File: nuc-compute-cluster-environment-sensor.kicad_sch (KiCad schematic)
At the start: 122 parts, among them J15 USB-C_GCT_USB4105-GF-A, J16 JST_SH_1x4_SM04B-SRSS-TB-LF-SN, J17 JST_SH_1x4_SM04B-SRSS-TB-LF-SN, U24 FT4232H_VQFN, U25 AP7370-33SA-7, U26 STM32G474CET6, U27 MB85RC1MTPNF-G, U28 SHT45, U29 BME280, Y2 Resonator_12MHz_ABM3B, Y3 Resonator_32.768kHz_ABS06, Y4 Resonator_8MHz_ABM3B

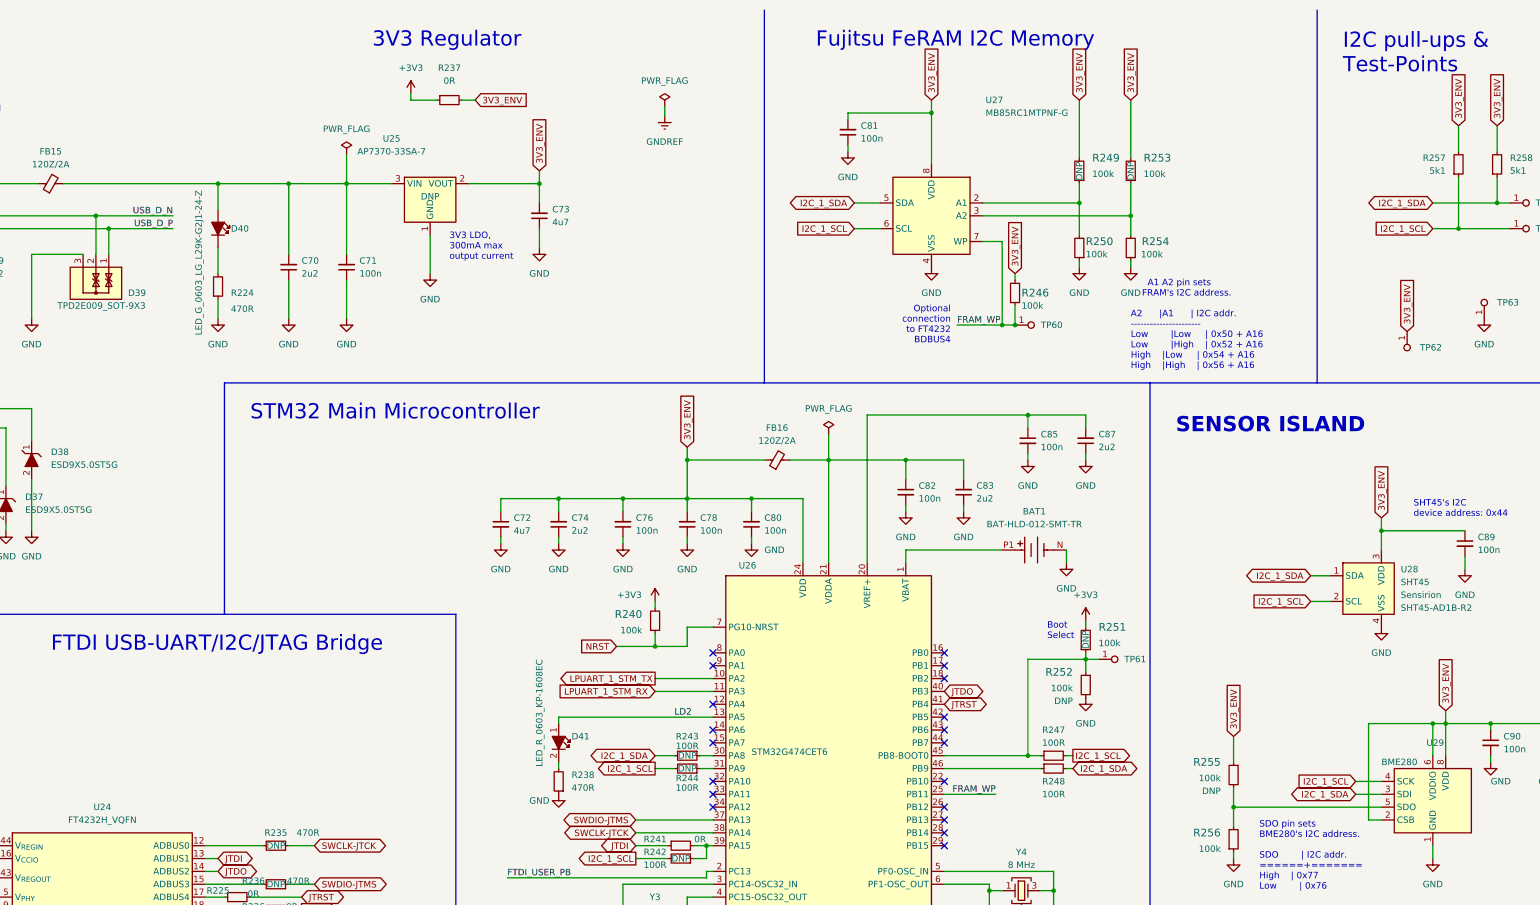
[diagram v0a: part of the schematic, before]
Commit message: Standarize all components and enumerate
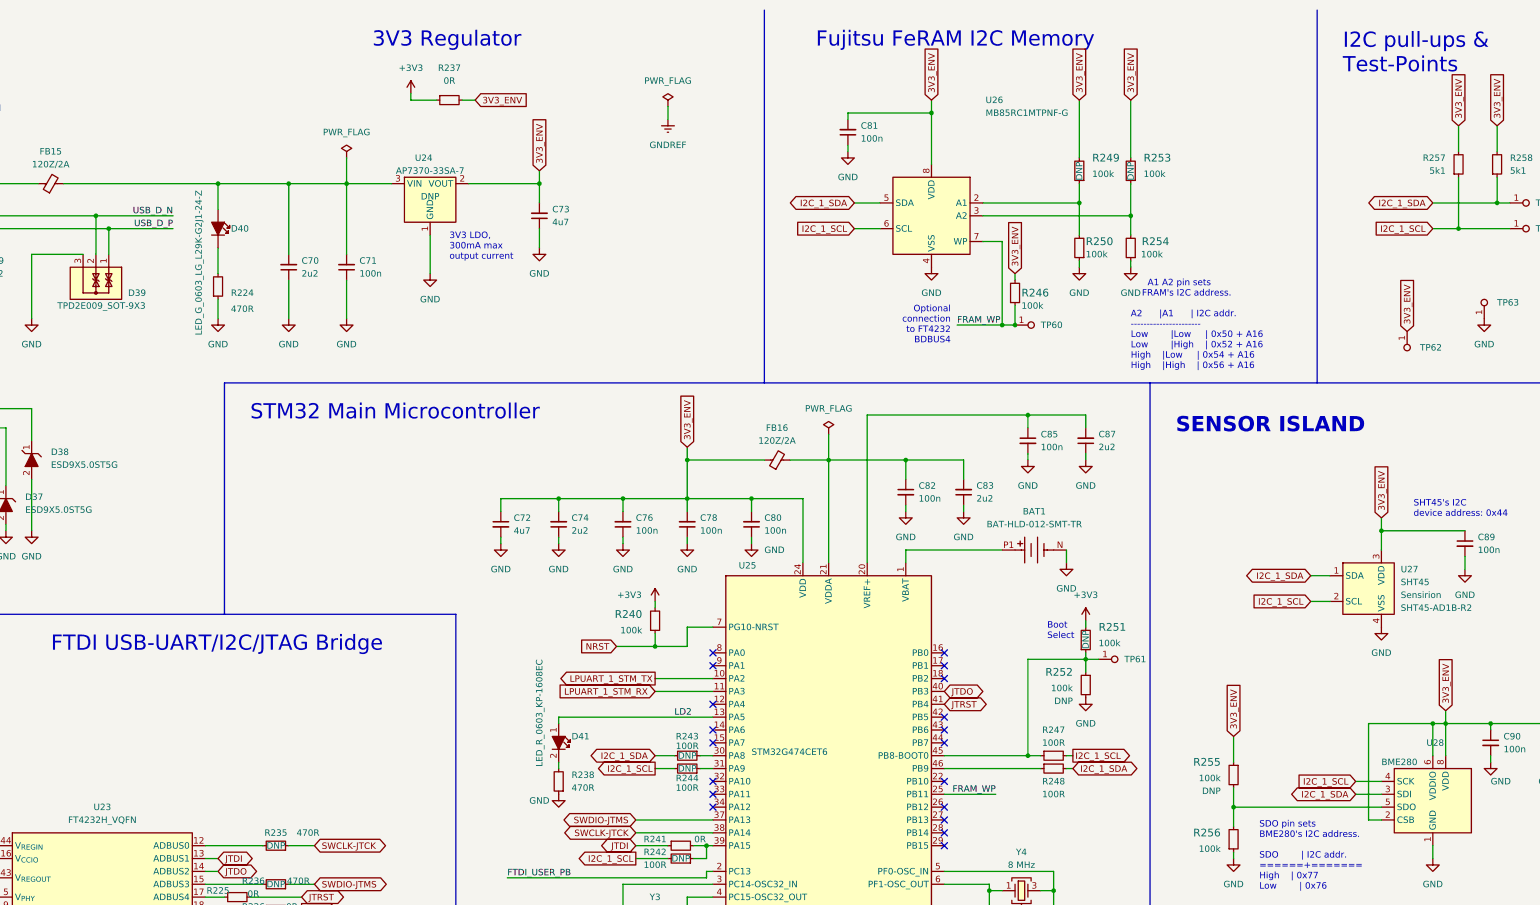
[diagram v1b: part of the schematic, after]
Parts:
- renumbered U24 to U23, U25 to U24, U26 to U25, U27 to U26, U28 to U27, U29 to U28

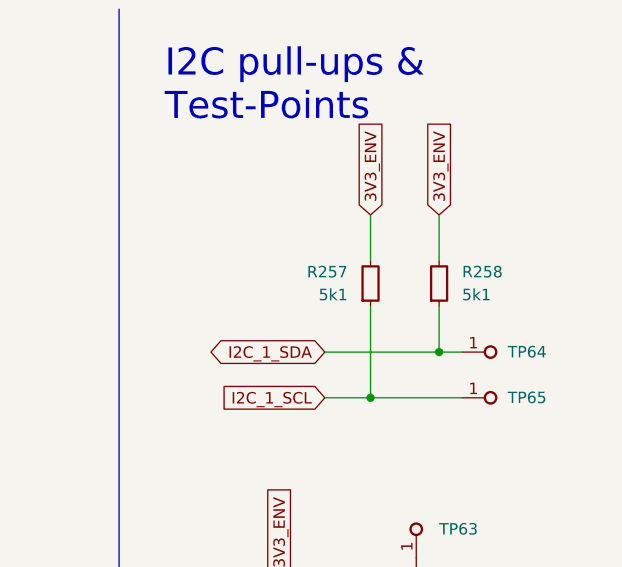
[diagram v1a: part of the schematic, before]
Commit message: Add fan arbiters for all outputs
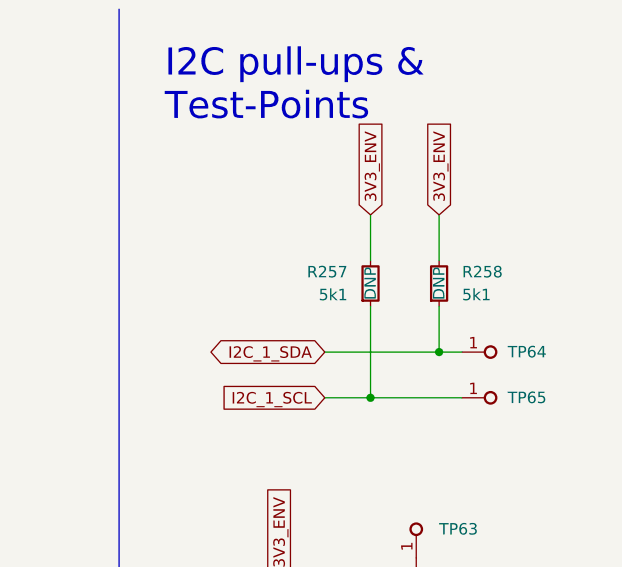
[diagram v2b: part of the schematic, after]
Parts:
- R257, R258: DNP (none) -> DNP
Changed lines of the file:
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@@
   )
   (symbol (lib_name "R_5k1_0402_3") (lib_id "antmicroResistors0402:R_5k1_0402") (at 381 45.72 90) (unit 1)
-    (in_bom yes) (on_board yes) (fields_autoplaced)
+    (in_bom yes) (on_board yes)
     (property "Reference" "R257" (id 0) (at 378.46 41.9099 90)
       (effects (font (size 1.27 1.27)) (justify left))
@@
       (effects (font (size 1.27 1.27)) (justify left bottom) hide)
     )
+    (property "DNP" "DNP" (id 10) (at 381 43.18 0))
     (pin "1")
     (pin "2")
@@
   )
   (symbol (lib_id "antmicroResistors0402:R_5k1_0402") (at 388.62 45.72 90) (unit 1)
-    (in_bom yes) (on_board yes) (fields_autoplaced)
+    (in_bom yes) (on_board yes)
     (property "Reference" "R258" (id 0) (at 391.16 41.9099 90)
       (effects (font (size 1.27 1.27)) (justify right))
@@
       (effects (font (size 1.27 1.27)) (justify left bottom) hide)
     )
-    (pin "1")
-    (pin "2")
+    (property "DNP" "DNP" (id 10) (at 388.62 43.18 0))
+    (pin "1")
+    (pin "2")

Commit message: Reannotate
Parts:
- renumbered C52 to C55, C53 to C56, C54 to C57, C55 to C58, C56 to C59, C57 to C60, C58 to C61, C59 to C62, C60 to C63, C61 to C64, C62 to C65, C63 to C66, C64 to C67, C65 to C68, C66 to C69, C67 to C70, C68 to C71, C69 to C72, C70 to C73, C71 to C74, C72 to C75, C73 to C76, C74 to C77, C75 to C78, C76 to C79, C77 to C80, C78 to C81, C79 to C82, C80 to C83, C81 to C84, C82 to C85, C83 to C86, C84 to C87, C85 to C88, C86 to C89, C87 to C90, C88 to C91, C89 to C92, C90 to C93, C91 to C94, R218 to R226, R219 to R227, R220 to R228, R221 to R229, R222 to R230, R223 to R231, R224 to R232, R225 to R233, R226 to R234, R227 to R235, R228 to R236, R229 to R237, R230 to R238, R231 to R239, R232 to R240, R233 to R241, R234 to R242, R235 to R243, R236 to R244, R237 to R245, R238 to R246, R239 to R247, R240 to R248, R241 to R249, R242 to R250, R243 to R251, R244 to R252, R245 to R253, R246 to R254, R247 to R255, R248 to R256, R249 to R257, R250 to R258, R251 to R259, R252 to R260, R253 to R261, R254 to R262, R255 to R263, R256 to R264, R257 to R265, R258 to R266, U23 to U26, U24 to U27, U25 to U28, U26 to U29, U27 to U30, U28 to U31

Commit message: Additional cleanup
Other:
- title: Server Case Temperature/Humidity Sensor -> GPU Cluster Backplane
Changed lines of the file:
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@@
   (paper "A3")
   (title_block
-    (title "Server Case Temperature/Humidity Sensor")
-    (date "2022-12-27")
+    (title "GPU Cluster Backplane")
+    (date "2023-10-18")
     (rev "1.0.0")
     (company "Antmicro Ltd")
     (comment 1 "www.antmicro.com")
+    (comment 2 "Antmicro Ltd.")
   )
   (junction (at 36.83 156.21) (diameter 0) (color 0 0 0 0)

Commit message: Minor fixes in schematic layout and reannotate
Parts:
- renumbered C55 to C56, C56 to C57, C57 to C58, C58 to C59, C59 to C60, C60 to C61, C61 to C62, C62 to C63, C63 to C64, C64 to C65, C65 to C66, C66 to C67, C67 to C68, C68 to C69, C69 to C70, C70 to C71, C71 to C72, C72 to C73, C73 to C74, C74 to C75, C75 to C76, C76 to C77, C77 to C78, C78 to C79, C79 to C80, C80 to C81, C81 to C82, C82 to C83, C83 to C84, C84 to C85, C85 to C86, C86 to C87, C87 to C88, C88 to C89, C89 to C90, C90 to C91, C91 to C92, C92 to C93, C93 to C94, C94 to C95, D35 to D36, D36 to D37, D37 to D38, D38 to D39, D39 to D40, D40 to D41, D41 to D42, D42 to D43, D43 to D44, D44 to D45, D45 to D46, FB12 to FB13, FB13 to FB14, FB14 to FB15, FB15 to FB16, FB16 to FB17, J15 to J17, J16 to J18, J17 to J19, R226 to R243, R227 to R244, R228 to R245, R229 to R246, R230 to R247, R231 to R248, R232 to R249, R233 to R250, R234 to R251, R235 to R252, R236 to R253, R237 to R254, R238 to R255, R239 to R256, R240 to R257, R241 to R258, R242 to R259, R243 to R260, R244 to R261, R245 to R262, R246 to R263, R247 to R264, R248 to R265, R249 to R266, R250 to R267, R251 to R268, R252 to R269, R253 to R270, R254 to R271, R255 to R272, R256 to R273, R257 to R274, R258 to R275, R259 to R276, R260 to R277, R261 to R278, R262 to R279, R263 to R280, R264 to R281, R265 to R282, R266 to R283, TP57 to TP60, TP58 to TP61, TP59 to TP62, TP60 to TP63, TP61 to TP64, TP62 to TP65, TP63 to TP66, TP64 to TP67, TP65 to TP68, U26 to U27, U27 to U28, U28 to U29, U29 to U30, U30 to U31, U31 to U32
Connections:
- no-connect marks 47 -> 50

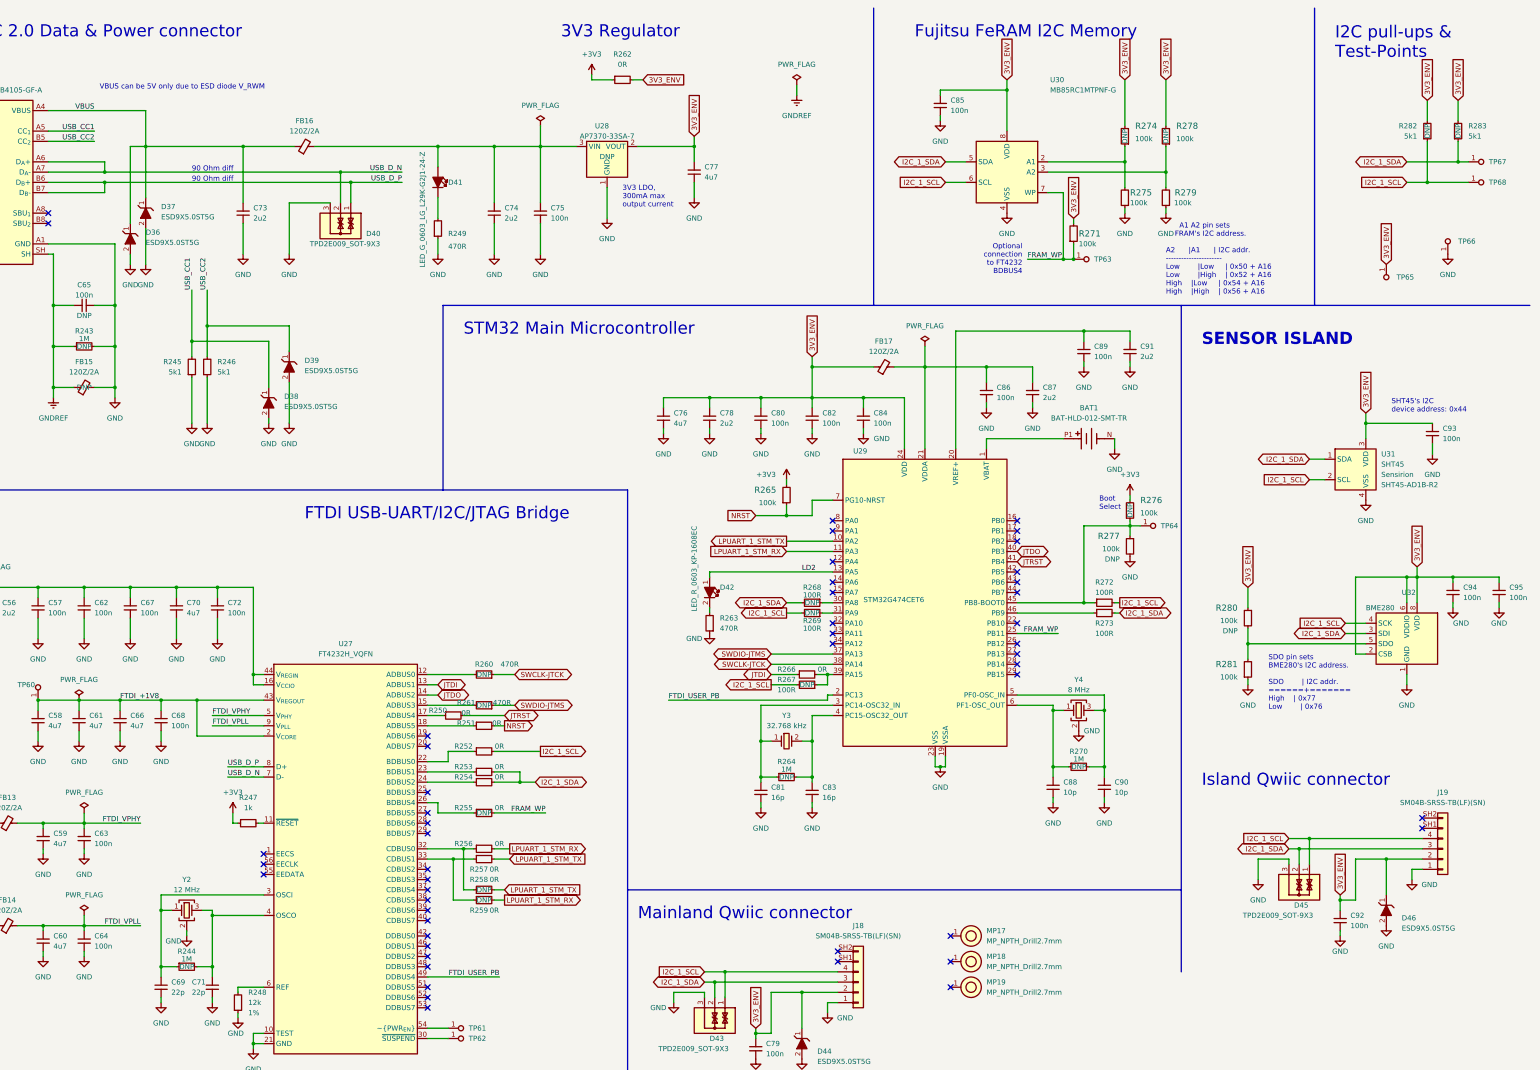
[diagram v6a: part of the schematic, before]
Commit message: Placement of supply section on PCB
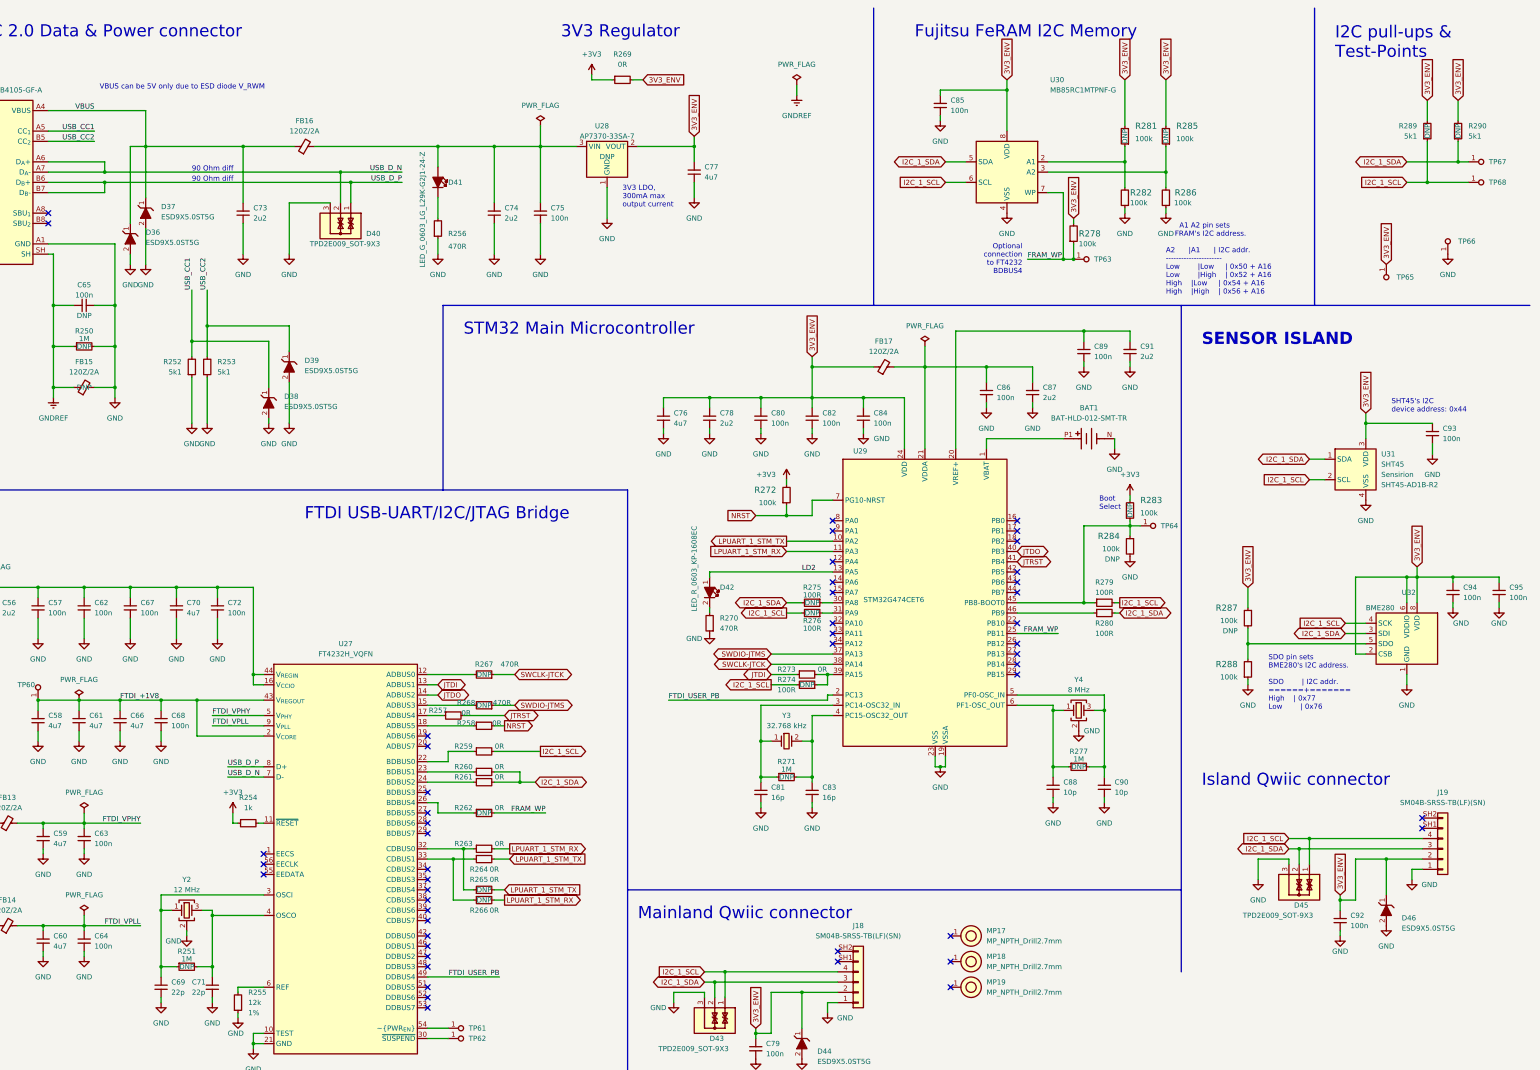
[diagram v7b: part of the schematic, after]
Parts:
- renumbered R243 to R250, R244 to R251, R245 to R252, R246 to R253, R247 to R254, R248 to R255, R249 to R256, R250 to R257, R251 to R258, R252 to R259, R253 to R260, R254 to R261, R255 to R262, R256 to R263, R257 to R264, R258 to R265, R259 to R266, R260 to R267, R261 to R268, R262 to R269, R263 to R270, R264 to R271, R265 to R272, R266 to R273, R267 to R274, R268 to R275, R269 to R276, R270 to R277, R271 to R278, R272 to R279, R273 to R280, R274 to R281, R275 to R282, R276 to R283, R277 to R284, R278 to R285, R279 to R286, R280 to R287, R281 to R288, R282 to R289, R283 to R290

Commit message: Implement changes suggested in schematic review
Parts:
- removed C58: C_4u7_0402, antmicro-footprints:C_0402_1005Metric, symbol antmicroCapacitors0402:C_4u7_0402
- removed C61, C66: C_100n_0402, antmicro-footprints:C_0402_1005Metric, symbol antmicroCapacitors0402:C_4u7_0402
- removed C92: C_100n_0402, antmicro-footprints:C_0402_1005Metric, symbol antmicroCapacitors0402:C_100n_0402
- removed D45: TPD2E009_SOT-9X3, antmicro-footprints:SOT-723, symbol antmicroTVSDiodes:TPD2E009_SOT-9X3
- removed D46: ESD9X5.0ST5G, antmicro-footprints:SOD-923, symbol antmicroTVSDiodes:ESD9X5.0ST5G
- removed J19: JST_SH_1x4_SM04B-SRSS-TB-LF-SN, antmicro-footprints:Conn_JST_SH_1x4_SM04B-SRSS-TB-LF-SN, symbol antmicroWire2BoardConnectors:JST_SH_1x4_SM04B-SRSS-TB-LF-SN
- removed MP17, MP18, MP19: MP_NPTH_Drill2.7mm, antmicro-footprints:MP_NPTH_Drill2.7mm, symbol antmicroMechanicalParts:MP_NPTH_Drill2.7mm
- added C?: C_3u3_0402, antmicro-footprints:C_0402_1005Metric, symbol antmicroCapacitors0402:C_3u3_0402
- added R?: R_0R_0805, antmicro-footprints:R_0805_2012Metric, symbol antmicroResistorsmisc:R_0R_0805
- C68, R269: DNP (none) -> DNP
- R289, R290, U28: DNP DNP -> (none)
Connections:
- net 3V3_ENV: now also R?.2; no longer U28.2 (VOUT)
- net FTDI_+1V8: now also C?.2
- net GND: now also J18.SH1, J18.SH2, C?.1
- new net: R?.1, U28.2 (VOUT)
- no-connect marks 50 -> 43
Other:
- note removed: "Island Qwiic connector"
- note removed: "Mainland Qwiic connector"
- moved on the sheet: C81, C83, R257, TP60
